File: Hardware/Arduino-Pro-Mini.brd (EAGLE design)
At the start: 17.8 x 33 mm, 29 parts, among them Q1 8/16/20MHz, U1 ATMEGA328, U2 MIC5205

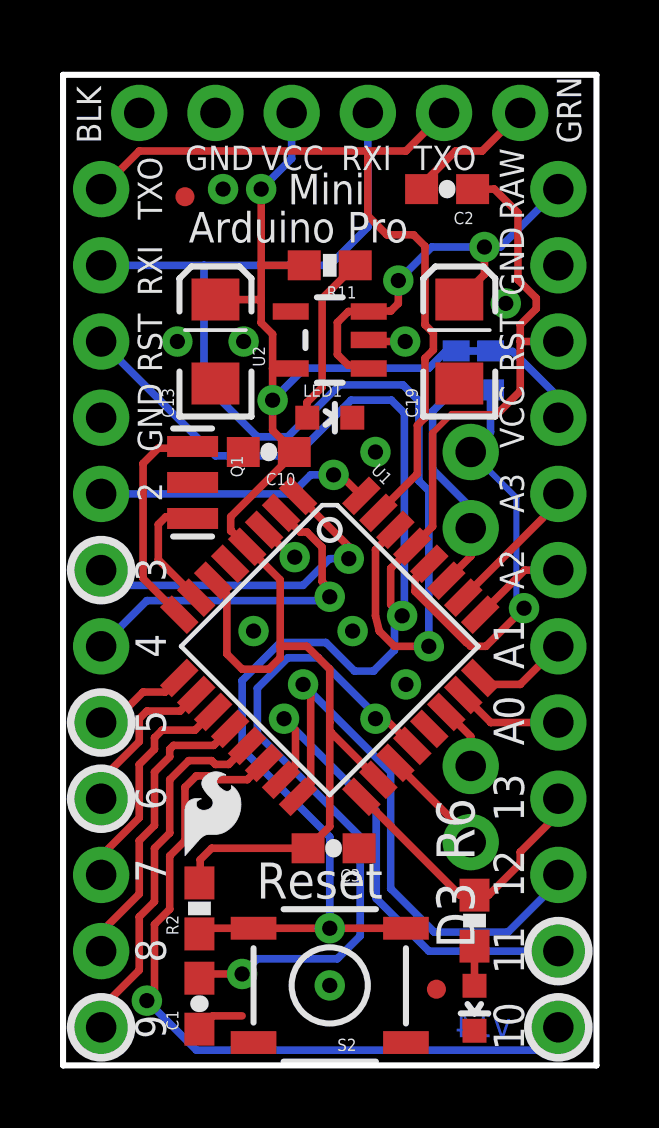
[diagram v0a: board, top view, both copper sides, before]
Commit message: Added power isolation jumper
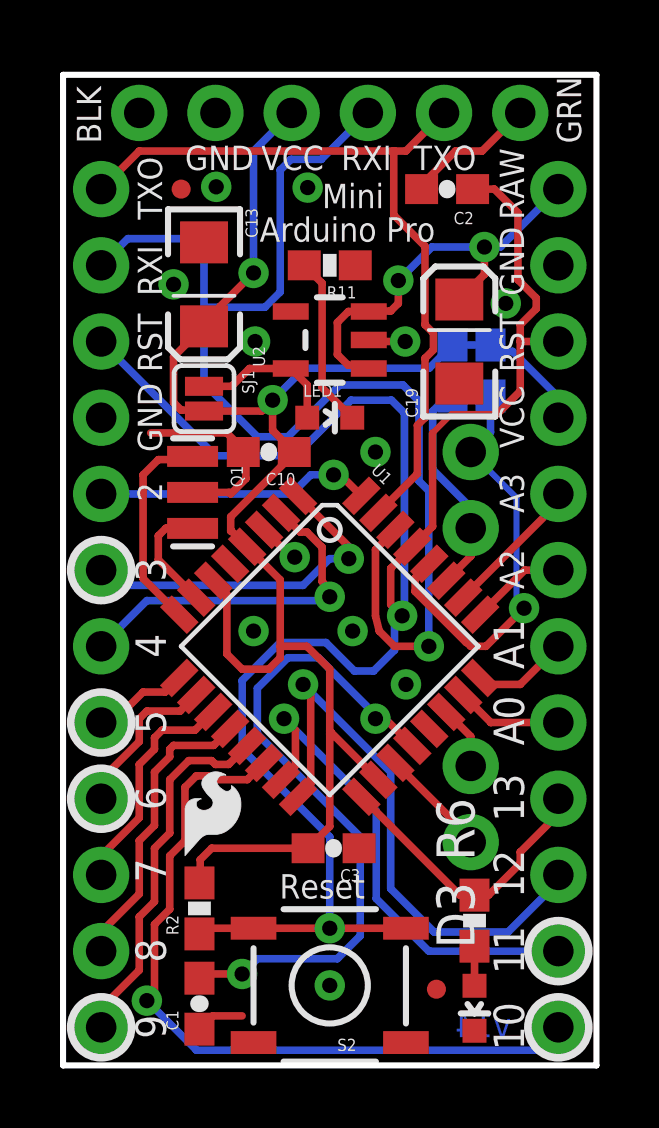
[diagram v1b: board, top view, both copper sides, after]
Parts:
- added SJ1: (no value), SparkFun-Passives:SJ_2S
- R1, R3: device SparkFun:0402-RES -> SparkFun:0603-RES
- moved C13 1.94 mm to (4.70, 26.0), turned to 270 degrees
- moved Q1 0.33 mm to (4.32, 19.1)
- moved JP5 0.28 mm to (3.94, 29.2)
- moved R1 0.13 mm to (13.0, 23.2)
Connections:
- removed net N$38: LED1.A, R11.1
- new net N$3: LED1.A, SJ1.1, U2.5
- new net N$4: LED1.C, R11.2
- net GND: now also R11.1; no longer LED1.C
- net VCC: now also SJ1.2; no longer R11.2, U2.5
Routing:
- net GND: track 4.80 -> 10.6 mm, vias 11 -> 12
- net N$38: track 5.76 -> 0.00 mm
- net N$4: track 0.00 -> 5.74 mm
- net N$3: track 0.00 -> 5.01 mm
- net RXI: track 39.8 -> 41.5 mm
- net VCC: track 55.9 -> 57.3 mm
- net TXO: track 26.7 -> 25.8 mm
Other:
- board text added: "Original Arduino Mini Design by Team Arduino Arduino Pro Mini Design by SparkFun Electronics Revised by Pete Lewis"
- board text removed: "Original Arduino Mini Design by Team Arduino Arduino Pro Mini Design by SparkFun Electronics"

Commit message: footprint updates, schematic work
-reset button, moved pads out for more toe
-resonator, 1:1 with fake traces
-moved all labels to flags in sch
-moved A6/A7 header to 2X1, rather than singles
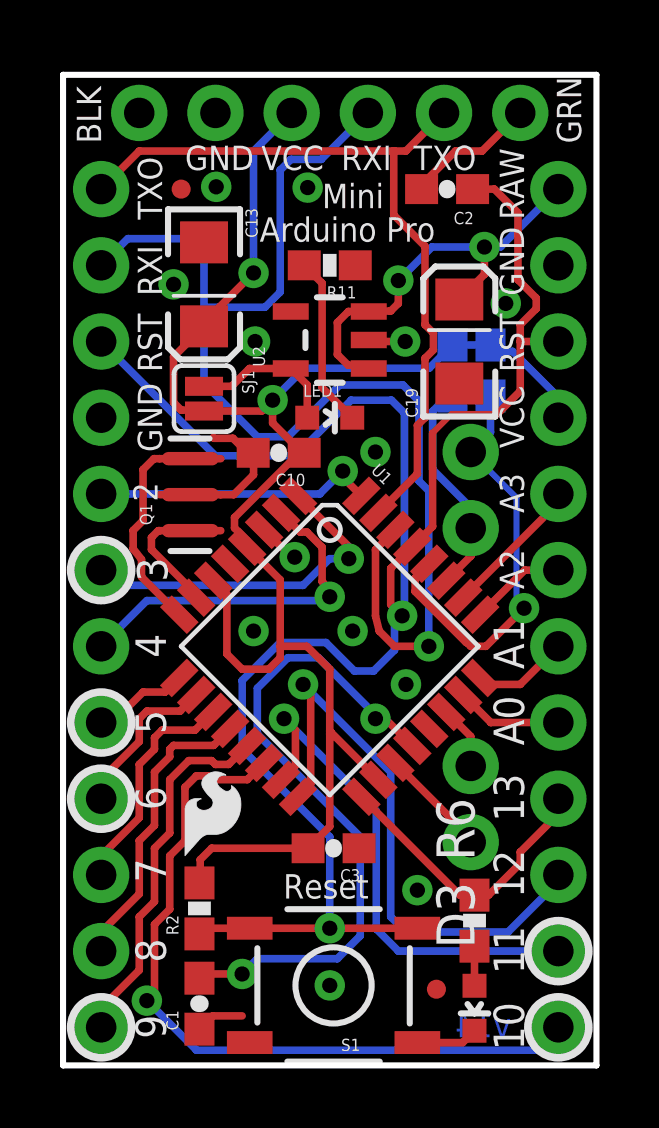
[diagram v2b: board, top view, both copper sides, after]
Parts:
- removed JP4: (no value), SparkFun:1X01
- removed S2: Reset, SparkFun:TACTILE_SWITCH_SMD
- added S1: Reset, Testing:TACTILE-SWITCH-SMD-ALT01
- JP3: device SparkFun:1X01 -> SparkFun:1X02
- Q1: device SparkFun:RESONATOR-SMD -> Testing:RESONATOR-SMD-1:1
- moved C10 0.33 mm to (7.19, 20.4)
- moved Q1 0.11 mm to (4.24, 19.0), turned to 90 degrees
- turned JP3 to 90 degrees
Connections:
- net A7: now also JP3.2; no longer JP4.1
- net GND: now also S1.1, S1.2; no longer S2.1, S2.2
- net N$1: now also Q1.3; no longer Q1.1
- net N$2: now also Q1.1; no longer Q1.3
- net RESET: now also S1.3, S1.4; no longer S2.3, S2.4
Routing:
- net N$1: track 7.52 -> 6.30 mm
- net GND: track 10.6 -> 9.92 mm, vias 12 -> 13
- net MOSI: track 16.5 -> 17.1 mm
- net MISO: track 19.2 -> 19.7 mm
